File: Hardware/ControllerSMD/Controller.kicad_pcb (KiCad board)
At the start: 2 copper layers, 35 x 124 mm, 61 parts, among them J1 8P8C, J2 LCD Header, J3 USB_B_Micro, J4 S88, J5 Screw_Terminal_01x05, SW1 Rotary_Encoder_Switch, SW2 SW_F0, SW3 SW_F1, SW4 SW_F2, SW5 SW_F3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

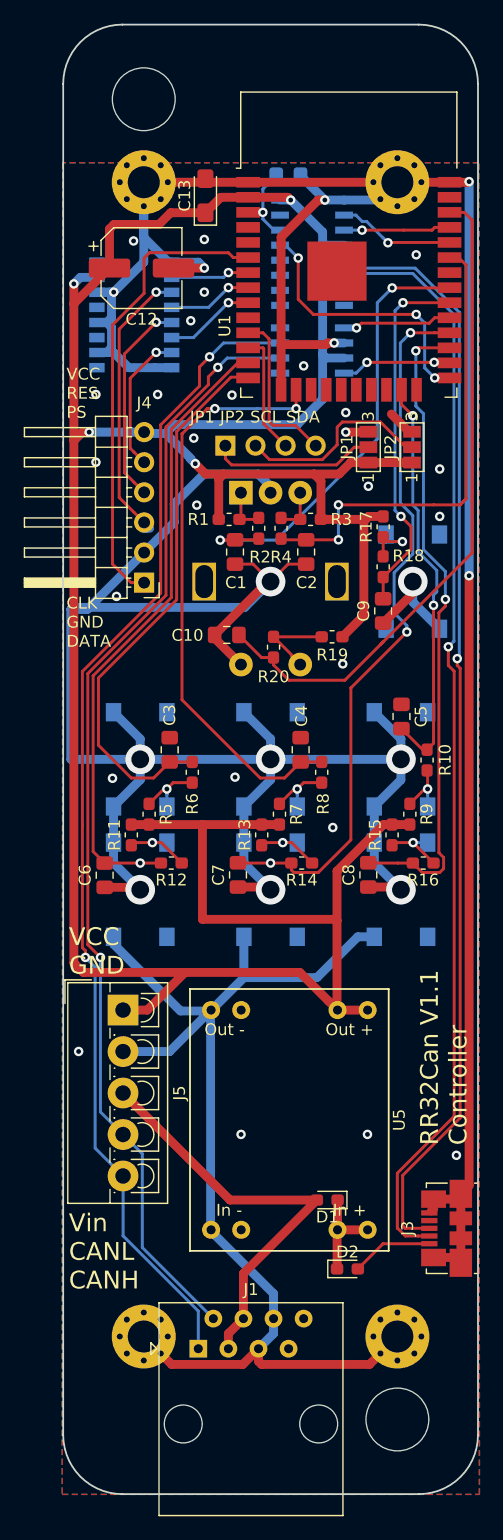
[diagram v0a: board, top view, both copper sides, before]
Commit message: Updated all boards
ESP32Breakout now with S88 driver.
ESP32Breakout has the auto-reset circut removed.
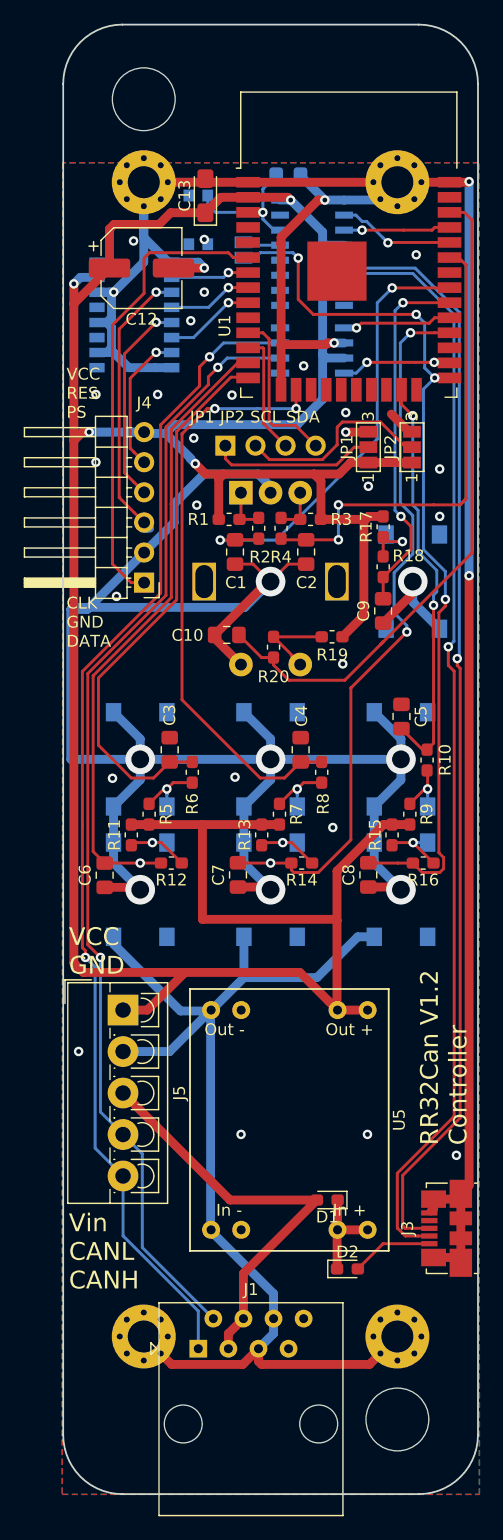
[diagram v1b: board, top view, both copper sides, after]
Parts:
- added JP3: Jumper_2_Open, Jumper:SolderJumper-2_P1.3mm_Open_Pad1.0x1.5mm, B.Cu at (29.2, 33.0)
- added SW9: EN, Button_Switch_SMD:SW_Push_1P1T_NO_CK_KMR2, B.Cu at (25.4, 30.5)
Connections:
- C8 pad 2: /Shift -> /GPIO0
- R16 pad 2: /Shift -> /GPIO0
- U1 pad 27: /Shift -> (no net)
- U4 pad 13: /GPIO0 -> /GPIO0-SER
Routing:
- net /Shift: track 54.9 -> 0.00 mm, vias 2 -> 0
- net /GPIO0: track 23.2 -> 76.0 mm, vias 3 -> 4
- net /EN: track 7.35 -> 13.0 mm, vias 1 -> 2
- net /GPIO0-SER: track 0.00 -> 3.19 mm
- net GND: vias 40 -> 39
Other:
- board text added: "RR32Can V1.2 Controller"
- board text removed: "RR32Can V1.1 Controller"
